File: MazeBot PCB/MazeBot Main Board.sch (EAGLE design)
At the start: 27 parts, among them IC1 7805TV, IC2 L298

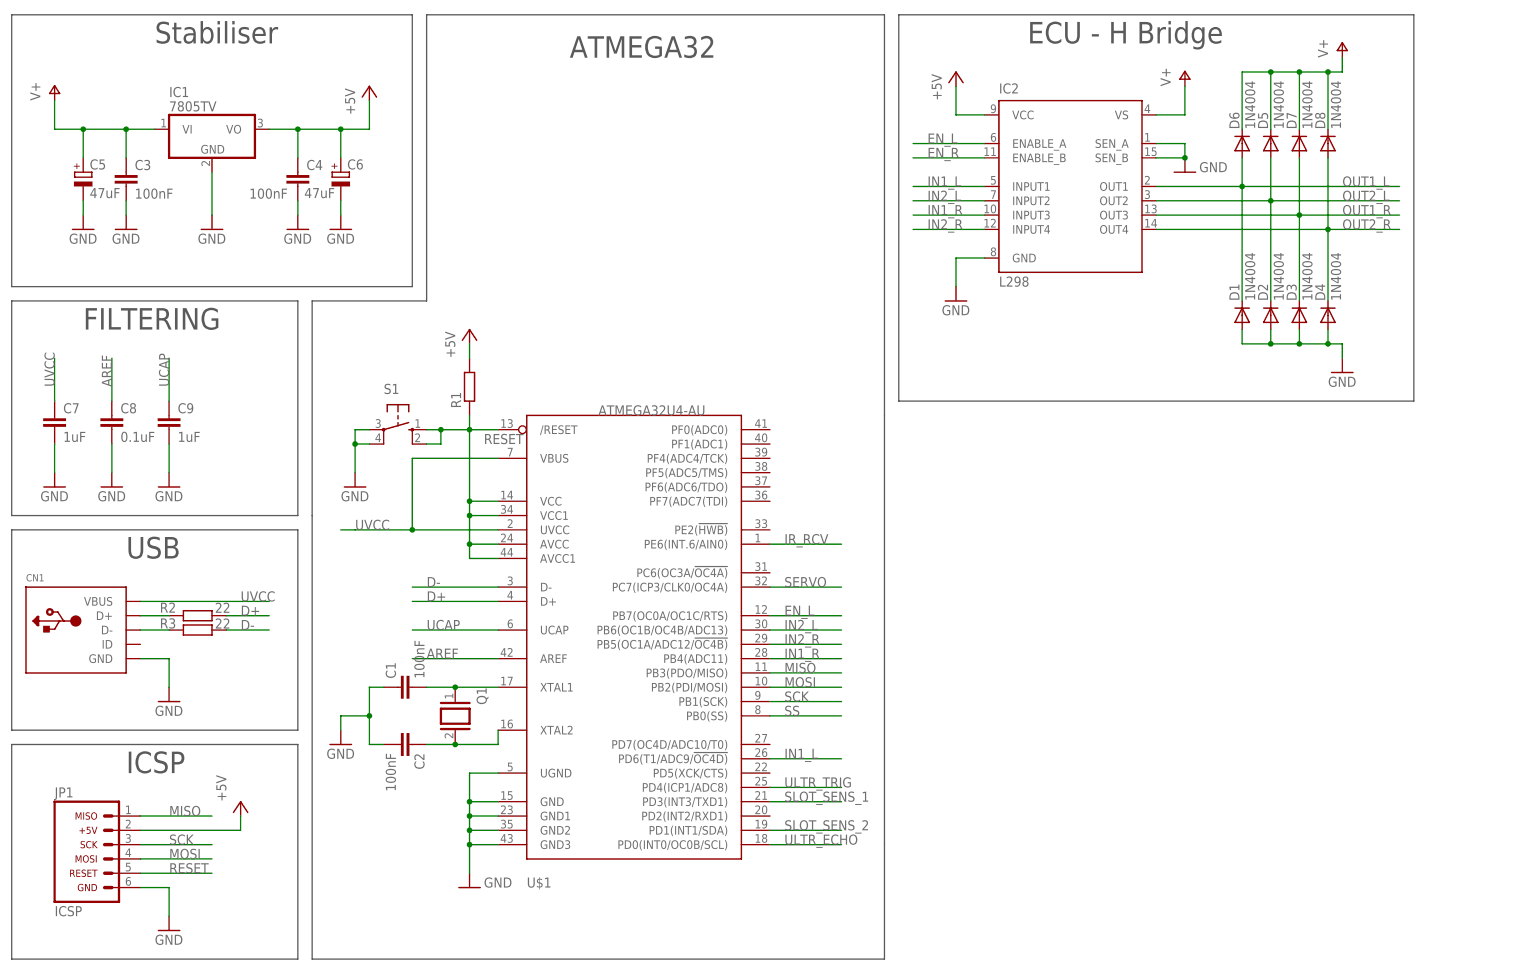
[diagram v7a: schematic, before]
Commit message: Add status diodes
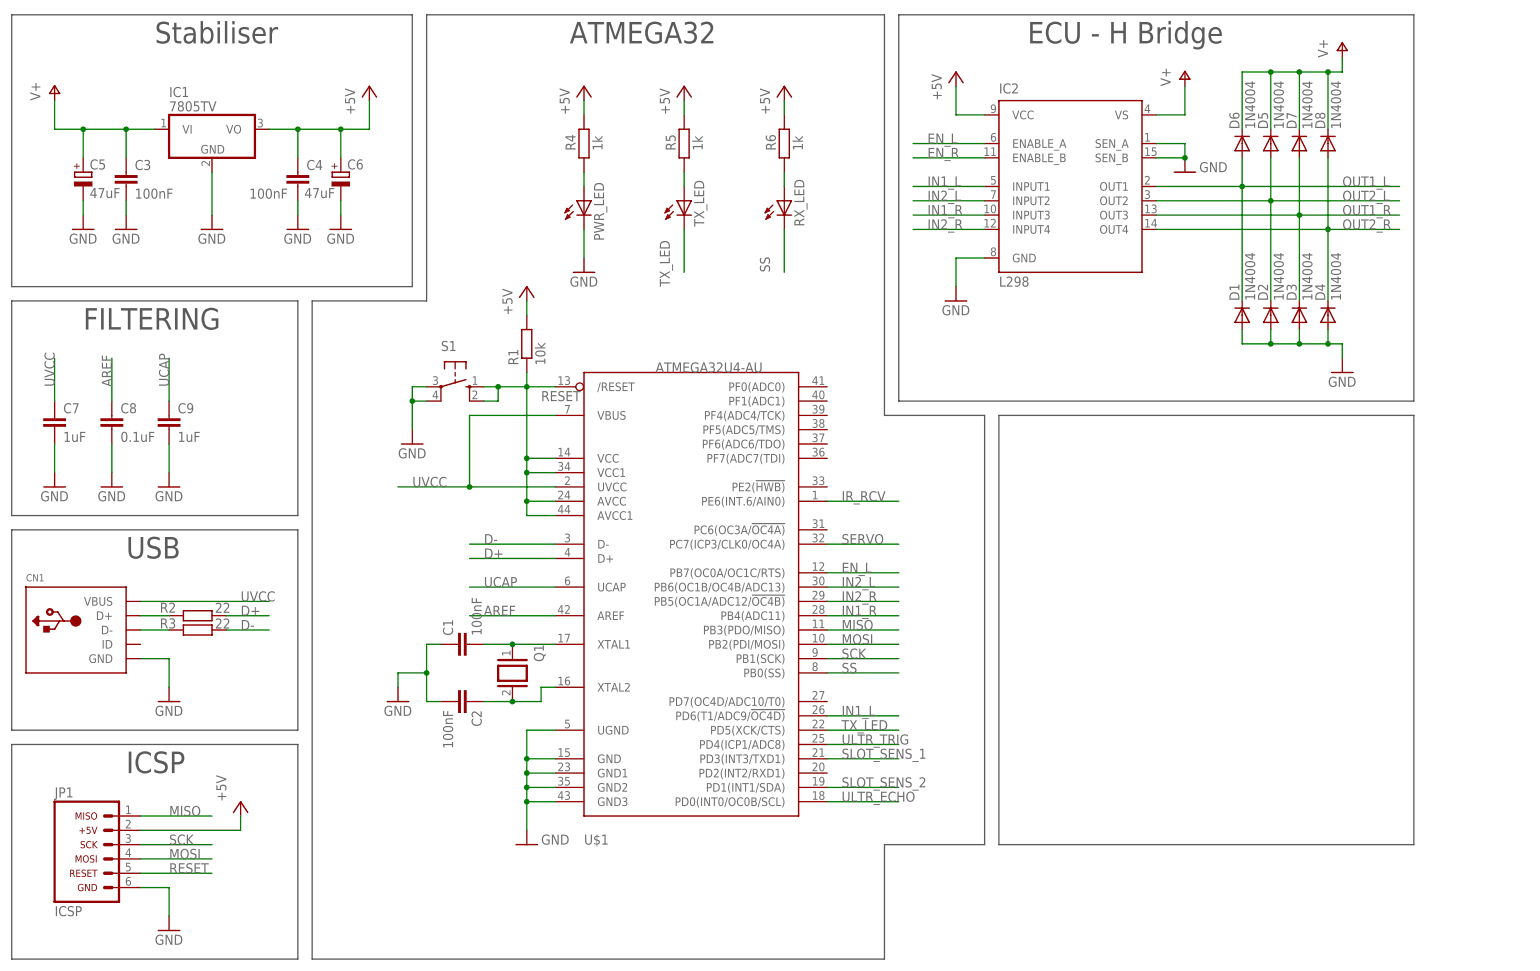
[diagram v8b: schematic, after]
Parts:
- added PWR_LED, RX_LED, TX_LED: (no value), led:LEDCHIP-LED0805
- added R4, R5, R6: 1k, rcl:R-EU_0207/10
- R1: value (none) -> 10k
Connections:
- new net N$3: PWR_LED.A, R4.1
- new net N$6: R5.1, TX_LED.A
- new net N$7: R6.1, RX_LED.A
- new net TX_LED: TX_LED.C, U$1.PD5(XCK/CTS)
- net +5V: now also R4.2, R5.2, R6.2
- net GND: now also PWR_LED.C
- net SS: now also RX_LED.C
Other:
- moved on the sheet: C1, C2, Q1, R1, S1, U$1
